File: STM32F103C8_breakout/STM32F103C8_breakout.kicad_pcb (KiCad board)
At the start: 2 copper layers, 70.8 x 42.5 mm, 34 parts, among them J1 Conn_01x18_Pin, J2 Conn_01x14_Pin, J20 USB-C, J21 Conn_01x02_Pin, U1 STM32F103C8T6, U2 BUCK_REG_3.3V, U3 GPTS203211B, Y1 16 MHz Crystal

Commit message: Connected Ferrite Bead + Fixed Cap. Values for Decoupling
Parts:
- C7 (x4): value 1μF -> 10μF
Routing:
- net Vdd: track 40.3 -> 41.8 mm, vias 6 -> 7
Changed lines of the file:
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@@
 			)
 		)
-		(property "Value" "1μF"
+		(property "Value" "10μF"
 			(at 3.4375 -0.015 0)
 			(layer "F.Fab")
@@
 		)
 		(fp_line
-			(start -5.170901 3.7255)
-			(end 5.170901 3.7255)
-			(stroke
-				(width 0.0254)
-				(type solid)
-			)
-			(layer "Edge.Cuts")
-		)
-		(fp_line
 			(start -5.170901 4.1529)
 			(end 5.170901 4.1529)
@@
 			)
 		)
-		(property "Value" "1μF"
+		(property "Value" "10μF"
 			(at 3.4375 -0.015 0)
 			(layer "F.Fab")
@@
 			)
 		)
-		(property "Value" "1μF"
+		(property "Value" "10μF"
 			(at 3.4375 -0.015 90)
 			(layer "F.Fab")
@@
 			)
 		)
-		(property "Value" "1μF"
+		(property "Value" "10μF"
 			(at 3.4375 -0.015 0)
 			(layer "F.Fab")
@@
 	)
 	(segment
+		(start 147 113.8)
+		(end 147 115.3)
+		(width 0.2)
+		(layer "F.Cu")
+		(net "Vdd")
+	)
+	(segment
 		(start 140.6625 90.7)
 		(end 142.6625 92.7)
@@
 		(size 0.6)
 		(drill 0.3)
+		(layers "F.Cu" "B.Cu")
+		(net "Vdd")
+	)
+	(via
+		(at 147 115.3)
+		(size 0.6)
+		(drill 0.3)

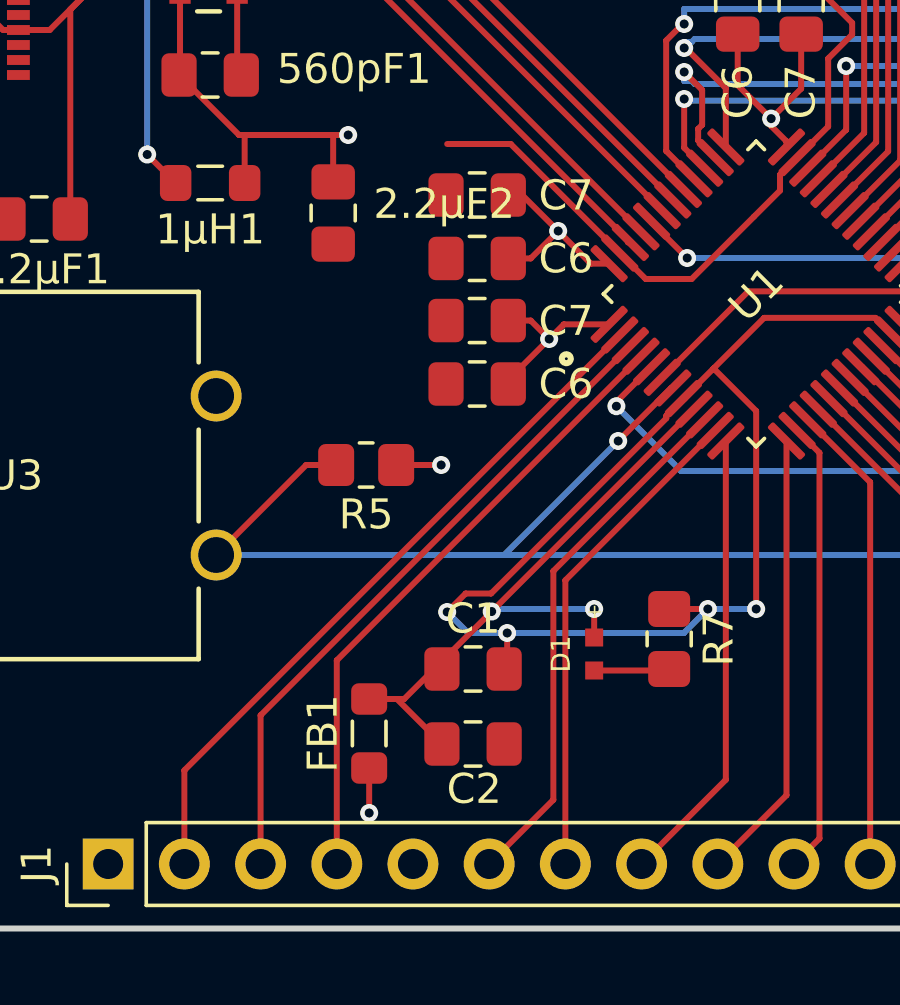
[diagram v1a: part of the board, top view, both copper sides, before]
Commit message: Filled Zones
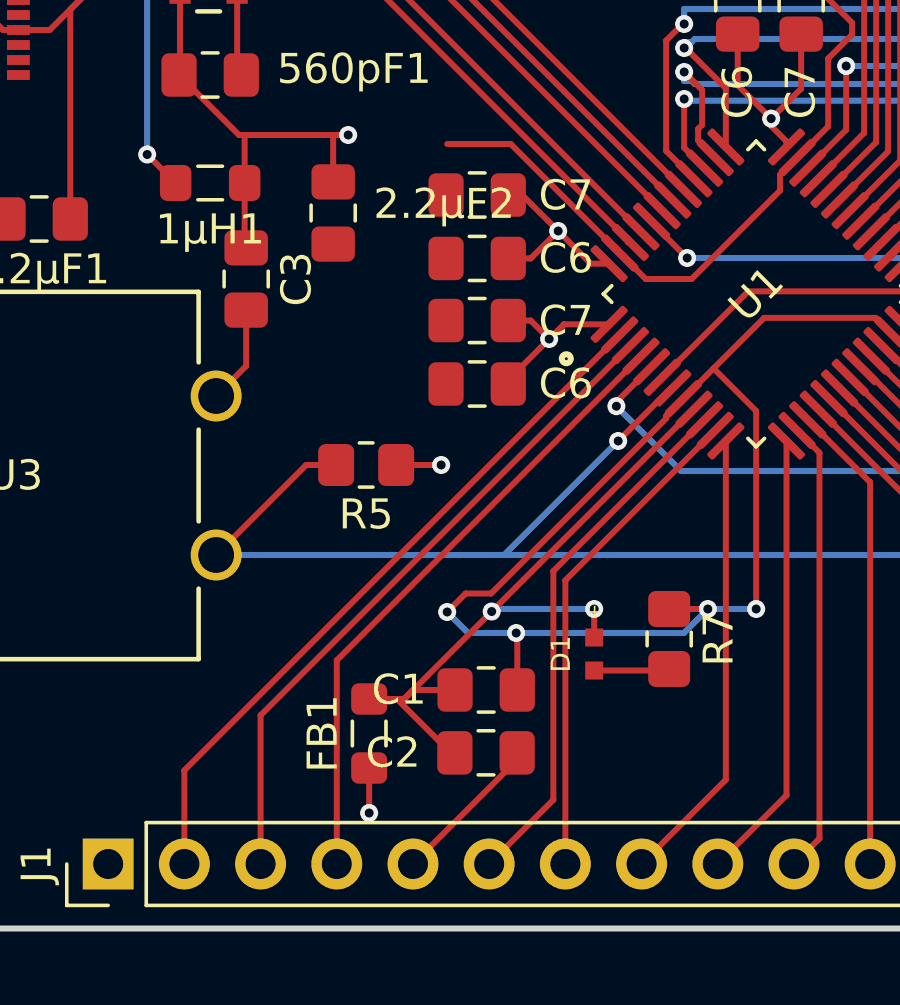
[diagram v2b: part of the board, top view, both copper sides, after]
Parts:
- added C3: 100nF, Capacitor_SMD:C_0805_2012Metric_Pad1.18x1.45mm_HandSolder, F.Cu at (142.9, 97.5)
- moved C1 0.83 mm to (150.9, 111.2)
- moved C2 0.52 mm to (150.9, 113.3)
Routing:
- net GNDREF: track 92.8 -> 101.9 mm
- net Vdd: track 41.8 -> 44.0 mm
- net Net-(U1-VDDA): track 22.3 -> 24.1 mm
